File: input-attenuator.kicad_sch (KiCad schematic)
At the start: 100 parts, among them J1 DC_INTF, J2 DC_INTF, J3 RX_1_RF, J4 RX_2_RF, J5 RF_IN, K1 EE2-5TNU-L, K2 EE2-5TNU-L, K3 EE2-5TNU-L, K4 EE2-5TNU-L, Q1 BC858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

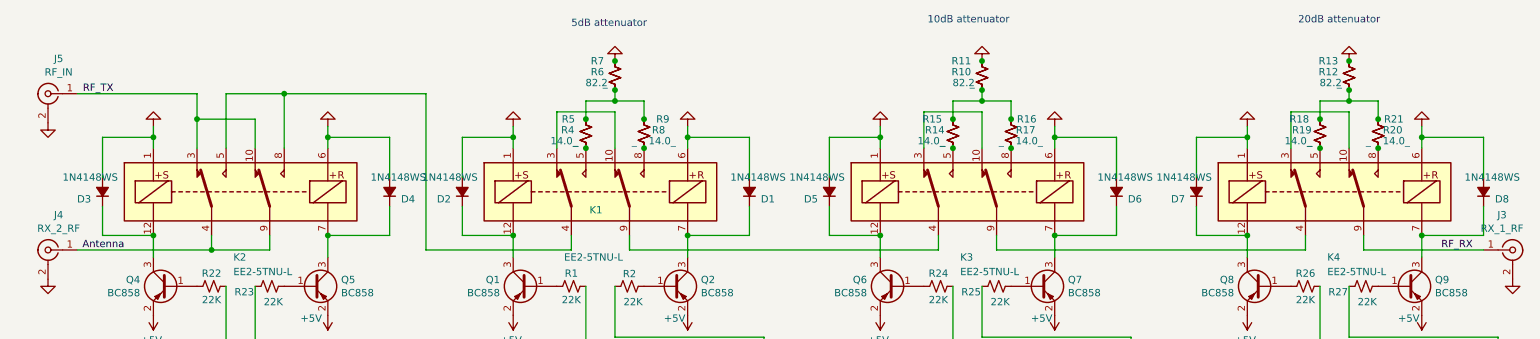
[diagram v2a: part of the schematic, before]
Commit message: Updated layout with inrush resistor
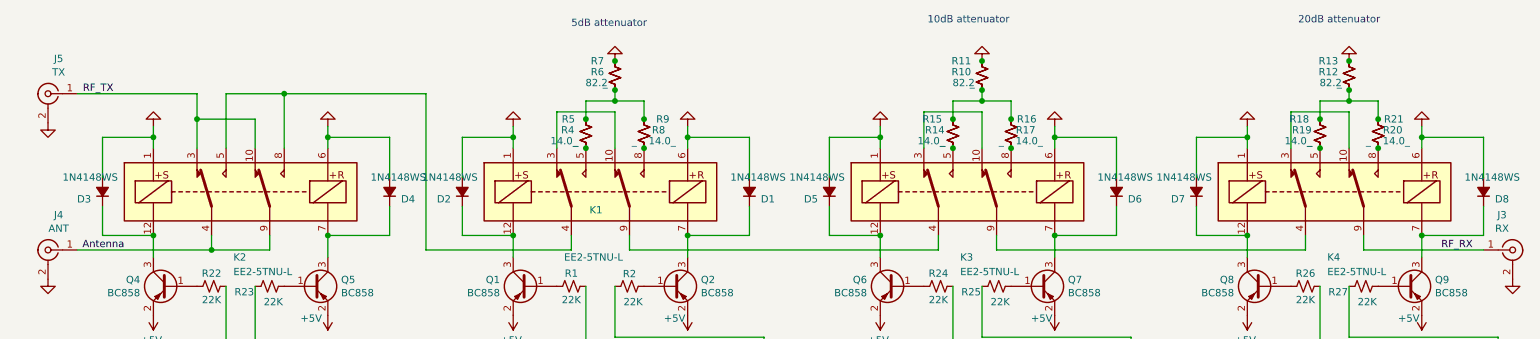
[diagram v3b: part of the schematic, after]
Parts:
- J3: value RX_1_RF -> RX
- J4: value RX_2_RF -> ANT
- J5: value RF_IN -> TX
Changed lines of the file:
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@@
     )
   )
-  (symbol (lib_id "power:PWR_FLAG") (at 163.83 170.18 270) (unit 1)
-    (in_bom yes) (on_board yes)
-    (property "Reference" "#FLG0101" (id 0) (at 165.735 170.18 0)
-      (effects (font (size 1.27 1.27)) hide)
-    )
-    (property "Value" "PWR_FLAG" (id 1) (at 168.275 170.18 90)
-      (effects (font (size 1.27 1.27)) (justify left) hide)
-    )
-    (property "Footprint" "" (id 2) (at 163.83 170.18 0)
-      (effects (font (size 1.27 1.27)) hide)
-    )
-    (property "Datasheet" "~" (id 3) (at 163.83 170.18 0)
-      (effects (font (size 1.27 1.27)) hide)
-    )
-    (pin "1")
-  )
-  (symbol (lib_id "power:PWR_FLAG") (at 163.83 172.72 270) (unit 1)
-    (in_bom yes) (on_board yes)
-    (property "Reference" "#FLG0102" (id 0) (at 165.735 172.72 0)
-      (effects (font (size 1.27 1.27)) hide)
-    )
-    (property "Value" "PWR_FLAG" (id 1) (at 168.275 172.72 90)
-      (effects (font (size 1.27 1.27)) (justify left) hide)
-    )
-    (property "Footprint" "" (id 2) (at 163.83 172.72 0)
-      (effects (font (size 1.27 1.27)) hide)
-    )
-    (property "Datasheet" "~" (id 3) (at 163.83 172.72 0)
-      (effects (font (size 1.27 1.27)) hide)
-    )
-    (pin "1")
-  )
   (symbol (lib_id "power:+5V") (at 38.1 71.12 180) (unit 1)
     (in_bom yes) (on_board yes)
@@
     (pin "1")
   )
+  (symbol (lib_id "power:PWR_FLAG") (at 163.83 170.18 270) (unit 1)
+    (in_bom yes) (on_board yes)
+    (property "Reference" "#FLG0101" (id 0) (at 165.735 170.18 0)
+      (effects (font (size 1.27 1.27)) hide)
+    )
+    (property "Value" "PWR_FLAG" (id 1) (at 168.275 170.18 90)
+      (effects (font (size 1.27 1.27)) (justify left) hide)
+    )
+    (property "Footprint" "" (id 2) (at 163.83 170.18 0)
+      (effects (font (size 1.27 1.27)) hide)
+    )
+    (property "Datasheet" "~" (id 3) (at 163.83 170.18 0)
+      (effects (font (size 1.27 1.27)) hide)
+    )
+    (pin "1")
+  )
+  (symbol (lib_id "power:PWR_FLAG") (at 163.83 172.72 270) (unit 1)
+    (in_bom yes) (on_board yes)
+    (property "Reference" "#FLG0102" (id 0) (at 165.735 172.72 0)
+      (effects (font (size 1.27 1.27)) hide)
+    )
+    (property "Value" "PWR_FLAG" (id 1) (at 168.275 172.72 90)
+      (effects (font (size 1.27 1.27)) (justify left) hide)
+    )
+    (property "Footprint" "" (id 2) (at 163.83 172.72 0)
+      (effects (font (size 1.27 1.27)) hide)
+    )
+    (property "Datasheet" "~" (id 3) (at 163.83 172.72 0)
+      (effects (font (size 1.27 1.27)) hide)
+    )
+    (pin "1")
+  )
   (symbol (lib_id "power:GND") (at 19.685 37.465 0) (unit 1)
     (in_bom yes) (on_board yes)
@@
     (pin "2")
   )
+  (symbol (lib_id "Comparator:LM339") (at 149.225 172.085 0) (unit 5)
+    (in_bom yes) (on_board yes)
+    (property "Reference" "U8" (id 0) (at 149.225 162.7948 0))
+    (property "Value" "LP339" (id 1) (at 149.225 165.093 0))
+    (property "Footprint" "Package_SO:SO-14_3.9x8.65mm_P1.27mm" (id 2) (at 147.955 169.545 0)
+      (effects (font (size 1.27 1.27)) hide)
+    )
+    (property "Datasheet" "https://www.st.com/resource/en/datasheet/lm139.pdf" (id 3) (at 150.495 167.005 0)
+      (effects (font (size 1.27 1.27)) hide)
+    )
+    (pin "12")
+    (pin "3")
+  )
   (symbol (lib_id "Device:D_Small_Filled") (at 29.21 49.53 270) (mirror x) (unit 1)
     (in_bom yes) (on_board yes)
@@
     (pin "1")
   )
-  (symbol (lib_id "Comparator:LM339") (at 149.225 172.085 0) (unit 5)
-    (in_bom yes) (on_board yes)
-    (property "Reference" "U8" (id 0) (at 149.225 162.7948 0))
-    (property "Value" "LP339" (id 1) (at 149.225 165.093 0))
-    (property "Footprint" "Package_SO:SO-14_3.9x8.65mm_P1.27mm" (id 2) (at 147.955 169.545 0)
-      (effects (font (size 1.27 1.27)) hide)
-    )
-    (property "Datasheet" "https://www.st.com/resource/en/datasheet/lm139.pdf" (id 3) (at 150.495 167.005 0)
-      (effects (font (size 1.27 1.27)) hide)
-    )
-    (pin "12")
-    (pin "3")
-  )
   (symbol (lib_id "Connector:Conn_Coaxial") (at 19.685 32.385 0) (mirror y) (unit 1)
     (in_bom yes) (on_board yes)
     (property "Reference" "J5" (id 0) (at 21.539 26.264 0))
-    (property "Value" "RF_IN" (id 1) (at 21.5392 28.6258 0))
+    (property "Value" "TX" (id 1) (at 21.5392 28.6258 0))
     (property "Footprint" "Connector_Coaxial:SMA_Amphenol_132134_Vertical" (id 2) (at 19.685 32.385 0)
       (effects (font (size 1.27 1.27)) hide)
@@
     (in_bom yes) (on_board yes)
     (property "Reference" "J4" (id 0) (at 21.5392 53.5686 0))
-    (property "Value" "RX_2_RF" (id 1) (at 21.5392 55.9308 0))
+    (property "Value" "ANT" (id 1) (at 21.5392 55.9308 0))
     (property "Footprint" "Connector_Coaxial:SMA_Amphenol_132134_Vertical" (id 2) (at 19.685 59.69 0)
       (effects (font (size 1.27 1.27)) hide)
@@
     (in_bom yes) (on_board yes)
     (property "Reference" "J3" (id 0) (at 273.7358 53.5686 0))
-    (property "Value" "RX_1_RF" (id 1) (at 273.7358 55.9308 0))
+    (property "Value" "RX" (id 1) (at 273.7358 55.9308 0))
     (property "Footprint" "Connector_Coaxial:SMA_Amphenol_132134_Vertical" (id 2) (at 275.59 59.69 0)
       (effects (font (size 1.27 1.27)) hide)
@@
     )
     (path "/00000000-0000-0000-0000-00005f287039"
-      (reference "J3") (unit 1) (value "RX_1_RF") (footprint "Connector_Coaxial:SMA_Amphenol_132134_Vertical")
+      (reference "J3") (unit 1) (value "RX") (footprint "Connector_Coaxial:SMA_Amphenol_132134_Vertical")
     )
     (path "/00000000-0000-0000-0000-00005f29dc0c"
-      (reference "J4") (unit 1) (value "RX_2_RF") (footprint "Connector_Coaxial:SMA_Amphenol_132134_Vertical")
+      (reference "J4") (unit 1) (value "ANT") (footprint "Connector_Coaxial:SMA_Amphenol_132134_Vertical")
     )
     (path "/5687a9c9-05f1-4ecb-9b08-f88b6a240510"
-      (reference "J5") (unit 1) (value "RF_IN") (footprint "Connector_Coaxial:SMA_Amphenol_132134_Vertical")
+      (reference "J5") (unit 1) (value "TX") (footprint "Connector_Coaxial:SMA_Amphenol_132134_Vertical")
     )
     (path "/00000000-0000-0000-0000-00005f18bdfb"

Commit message: Added regulator heat sink tab and module description on FCu
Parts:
- U7: footprint Package_TO_SOT_SMD:SOT-223-6 -> Package_TO_SOT_SMD:SOT-223-6_TabPin3
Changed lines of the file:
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@@
   (title_block
     (title "HF input attenuator")
-    (date "2020-07-21")
-    (rev "1.3")
+    (date "2021-03-22")
+    (rev "1.4")
     (company "Adrian Scripcă, Frédéric Boes")
   )
@@
     (property "Reference" "U7" (id 0) (at 108.585 115.316 0))
     (property "Value" "TPS7A4501DCQT" (id 1) (at 108.585 117.856 0))
-    (property "Footprint" "Package_TO_SOT_SMD:SOT-223-6" (id 2) (at 108.585 111.76 0)
+    (property "Footprint" "Package_TO_SOT_SMD:SOT-223-6_TabPin3" (id 2) (at 108.585 111.76 0)
       (effects (font (size 1.27 1.27)) hide)
     )
@@
     )
     (path "/8354ecd4-2a4f-44f8-a737-ff9cdb5f7927"
-      (reference "U7") (unit 1) (value "TPS7A4501DCQT") (footprint "Package_TO_SOT_SMD:SOT-223-6")
+      (reference "U7") (unit 1) (value "TPS7A4501DCQT") (footprint "Package_TO_SOT_SMD:SOT-223-6_TabPin3")
     )
     (path "/cb9337bf-8f82-4876-8c4b-170c9496f38f"

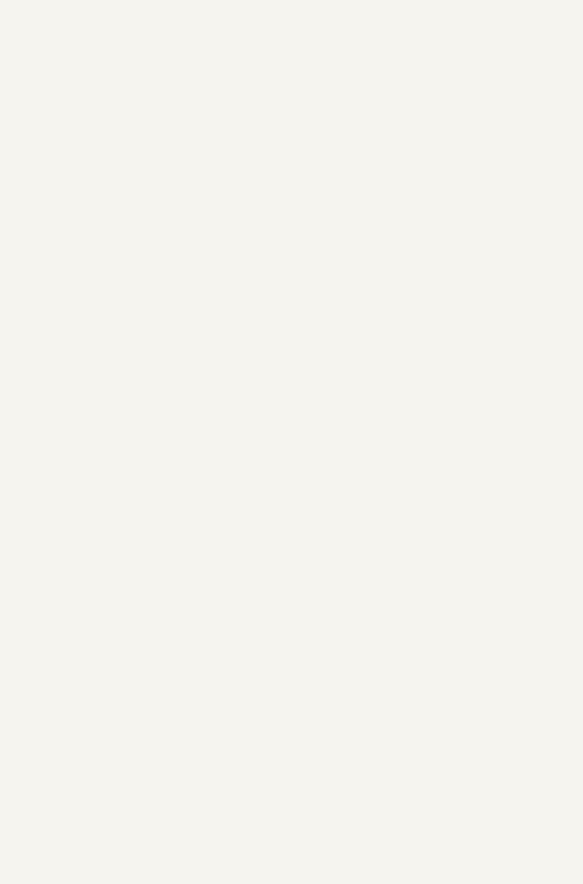
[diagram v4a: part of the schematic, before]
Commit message: Added an MCP23017
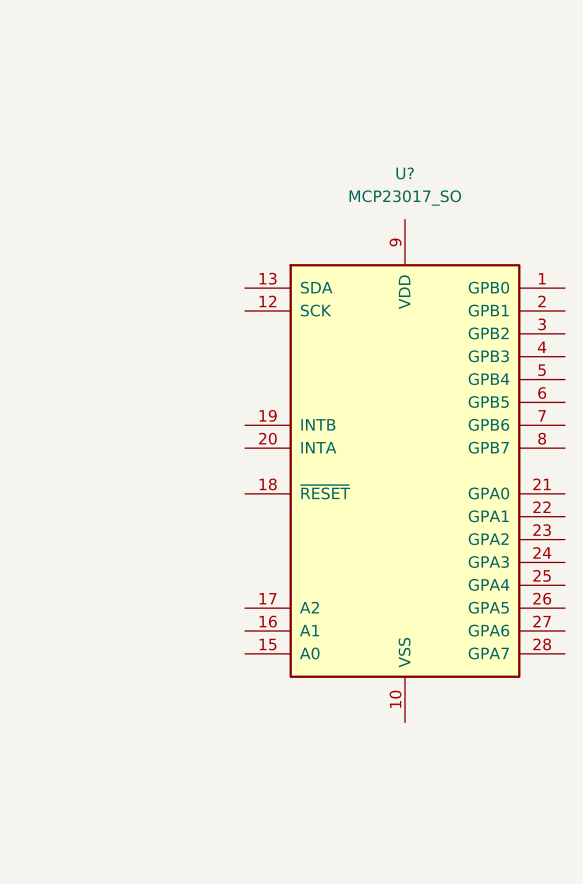
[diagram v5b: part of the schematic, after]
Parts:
- added U?: MCP23017_SO, Package_SO:SOIC-28W_7.5x17.9mm_P1.27mm, symbol Interface_Expansion:MCP23017_SO
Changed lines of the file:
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@@
-(kicad_sch (version 20210126) (generator eeschema)
+(kicad_sch (version 20210621) (generator eeschema)
   (paper "A4")
   (title_block
@@
     (pin "9")
   )
+  (symbol (lib_id "Interface_Expansion:MCP23017_SO") (at 320.675 129.54 0) (unit 1)
+    (in_bom yes) (on_board yes) (fields_autoplaced)
+    (property "Reference" "U?" (id 0) (at 320.675 96.52 0))
+    (property "Value" "MCP23017_SO" (id 1) (at 320.675 99.06 0))
+    (property "Footprint" "Package_SO:SOIC-28W_7.5x17.9mm_P1.27mm" (id 2) (at 325.755 154.94 0)
+      (effects (font (size 1.27 1.27)) (justify left) hide)
+    )
+    (property "Datasheet" "http://ww1.microchip.com/downloads/en/DeviceDoc/20001952C.pdf" (id 3) (at 325.755 157.48 0)
+      (effects (font (size 1.27 1.27)) (justify left) hide)
+    )
+    (pin "1")
+    (pin "10")
+    (pin "11")
+    (pin "12")
+    (pin "13")
+    (pin "14")
+    (pin "15")
+    (pin "16")
+    (pin "17")
+    (pin "18")
+    (pin "19")
+    (pin "2")
+    (pin "20")
+    (pin "21")
+    (pin "22")
+    (pin "23")
+    (pin "24")
+    (pin "25")
+    (pin "26")
+    (pin "27")
+    (pin "28")
+    (pin "3")
+    (pin "4")
+    (pin "5")
+    (pin "6")
+    (pin "7")
+    (pin "8")
+    (pin "9")
+  )
   (sheet_instances
     (path "/" (page "1"))
@@
       (reference "U8") (unit 5) (value "LP339") (footprint "Package_SO:SO-14_3.9x8.65mm_P1.27mm")
     )
+    (path "/4b62c546-cbc7-4118-9b7e-3c254506b7b9"
+      (reference "U?") (unit 1) (value "MCP23017_SO") (footprint "Package_SO:SOIC-28W_7.5x17.9mm_P1.27mm")
+    )
   )

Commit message: questionsForYou
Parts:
- removed U5: 74HC00, Package_SO:SO-14_3.9x8.65mm_P1.27mm, symbol 74xx:74HC00
- removed U6: 74HC595, Package_SO:SO-16_3.9x9.9mm_P1.27mm, symbol 74xx:74HC595
- added R52, R53, R54, R55, R56: 100k, Resistor_SMD:R_0805_2012Metric, symbol Device:R_Small_US
- added R59: 1M, Resistor_SMD:R_0805_2012Metric, symbol Device:R_Small_US
- added unit 2 of U8
- R33: value 1M -> 100k
- gave numbers to parts that had none: 1
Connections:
- net +5V: now also C2.1, U6.15 (A0), U6.9 (VDD), R52.2, R59.2, U8.7 (+); no longer C2.2
- net 10dB: now also R29.1, U2.1, U2.2, U2.9, U6.7 (GPB6), R55.1
- net 20dB: now also R30.1, U3.1, U3.2, U3.9, U6.8 (GPB7), R56.1
- net 5dB: now also R3.1, U1.1, U1.2, U1.9, U6.23 (GPA2), R54.1
- net GND: now also C2.2, R33.2, U6.10 (VSS), U6.16 (A1), R53.2, R54.2, R55.2, R56.2; no longer C2.1
- net PowerDn: no longer R33.1
- net Rx: now also R28.1, R33.1, U4.1, U4.2, U4.9, U6.21 (GPA0)
- net Vin2: no longer R33.2
- net at R1.1: now also U1.6; no longer U1.8
- net at R2.1: now also U1.8; no longer U1.6
- net SCL: now reaches J1.4 (Pin_4), J2.4 (Pin_4)
- net SCL: now also J1.6 (Pin_6), J2.5 (Pin_5), U6.12 (SCK)
- net SDA: now reaches J1.3 (Pin_3), J2.3 (Pin_3)
- net SDA: now also U6.13 (SDA)
- net at R27.1: now also U3.8; no longer U3.6
- net at U2.6: now also R24.1; no longer R25.1
- net at R26.1: now also U3.6; no longer U3.8
- net at U6.17 (A2): now also R52.1, R53.1
- net IIC_Reset: now reaches U6.18 (~{RESET})
- net IIC_Reset: now also R59.1, U8.1
- net at R22.1: now also U4.6; no longer U4.8
- net at R31.2, R32.1, R35.2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: now also U8.6 (-)
- net at R23.1: now also U4.8; no longer U4.6
- net at U2.8: now also R25.1; no longer R24.1
- no-connect marks 5 -> 13
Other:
- note added: "IO connectors and expander"
- note removed: "IO connectors and shift register"
- moved on the sheet: C1, C8, D10, H1, H2, H3, H4, U1E, U2E, U3E, U4E, U6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

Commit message: final
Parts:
- removed J2: DC_INTF, Connector_PinHeader_2.54mm:PinHeader_1x07_P2.54mm_Vertical, symbol Connector:Conn_01x07_Male
- removed R59: 1M, Resistor_SMD:R_0805_2012Metric, symbol Device:R_Small_US
- removed unit 2 of U8
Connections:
- net PowerDn is gone; now on net IIC_Reset: Q3.3 (C), R31.1, R36.1, U8.2
- net SCL: no longer J1.6 (Pin_6)
- net SHDN: now also J1.5 (Pin_5); no longer J1.7 (Pin_7)
- no-connect marks 13 -> 12
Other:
- note removed: "To next shift register"
- moved on the sheet: R33, R54, R55, R56
